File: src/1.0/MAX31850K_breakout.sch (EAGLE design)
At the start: 15 parts, among them J1 M08SQ1, U1 3.3V, U2 MAX31850K

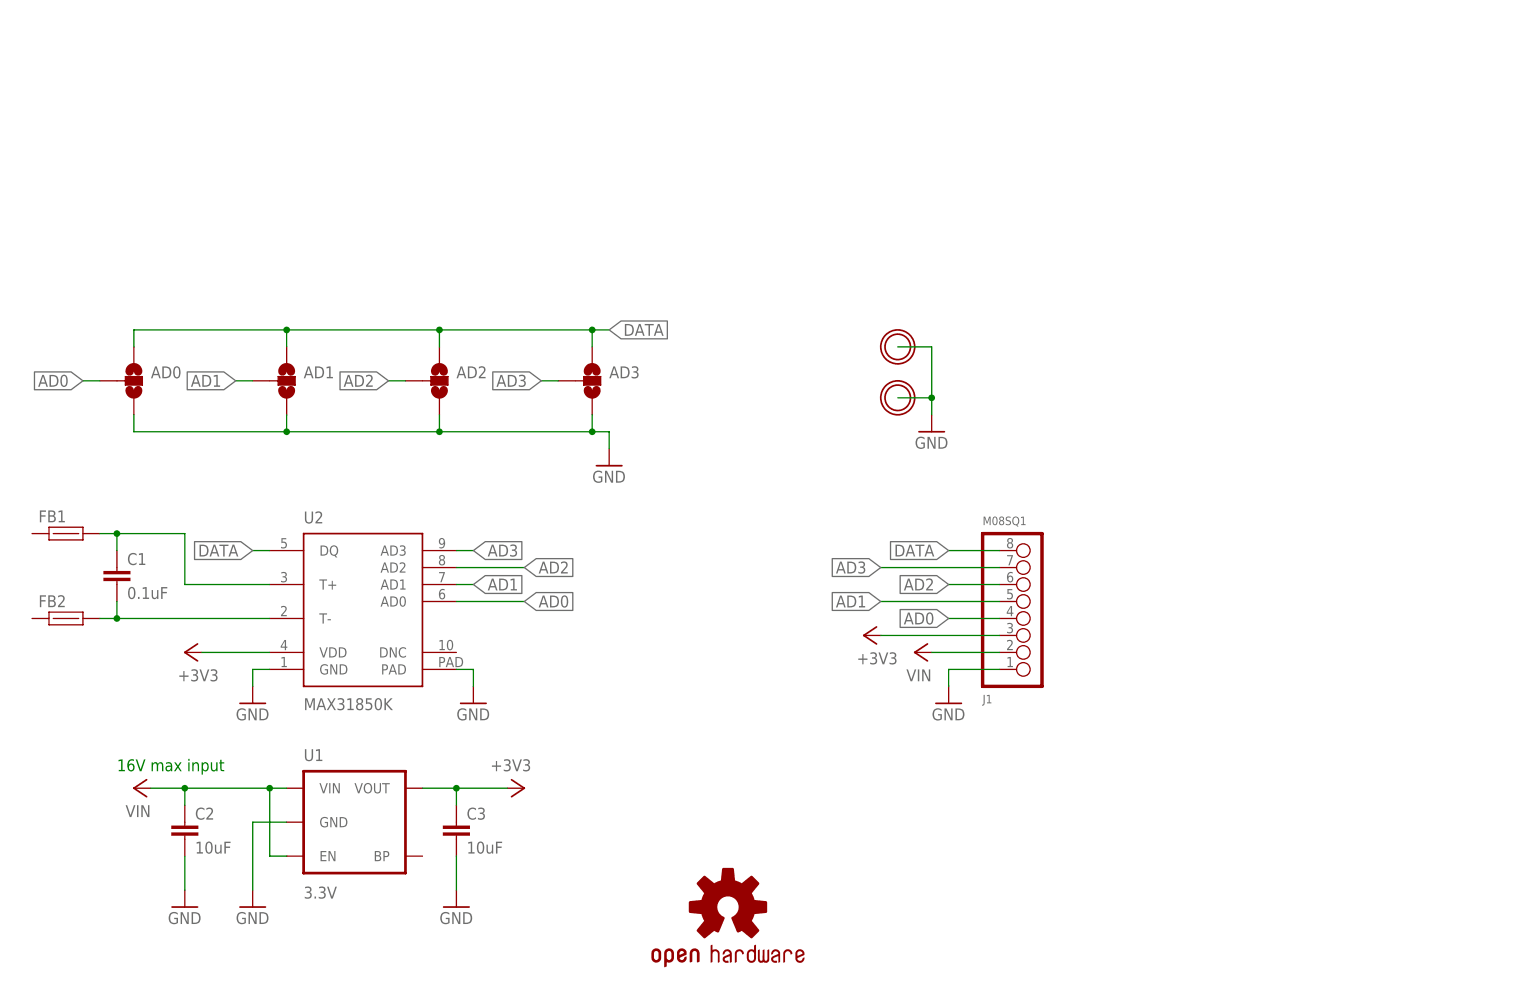
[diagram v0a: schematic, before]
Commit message: Updated file structure to match PCBGuidelines structure (still in development). Preparing to move to release candidate.
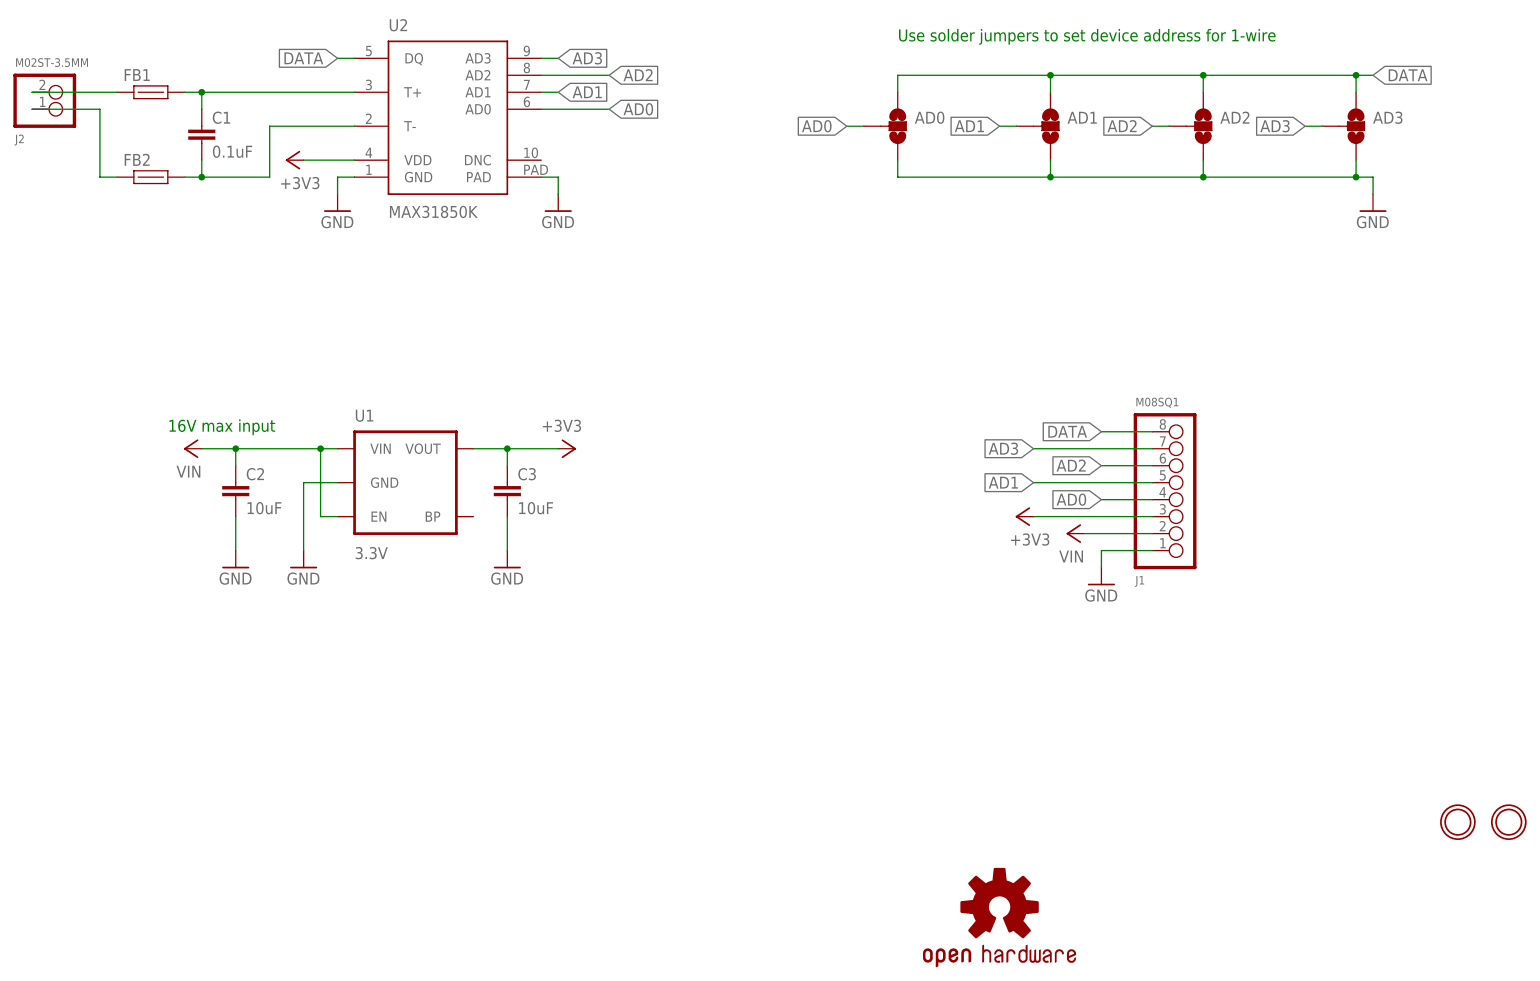
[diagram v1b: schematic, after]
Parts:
- added J2: M02ST-3.5MM, LoganSmith-Connectors:M02ST-3.5MM
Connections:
- new net TM_RAW: FB2.1, J2.1
- new net TP_RAW: FB1.1, J2.2
- net GND: no longer U$1.P$1, U$2.P$1
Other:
- note added: "Use solder jumpers to set device address for 1-wire"
- moved on the sheet: AD0, AD1, AD2, AD3, C1, C2, C3, FB1, FB2, J1, U1, U2

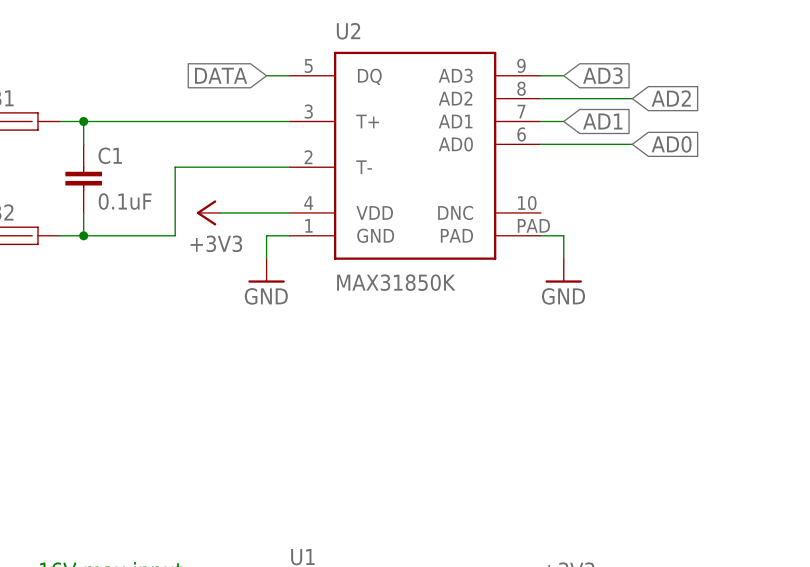
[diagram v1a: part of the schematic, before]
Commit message: Added BOM, still need part number for 1x8 header.
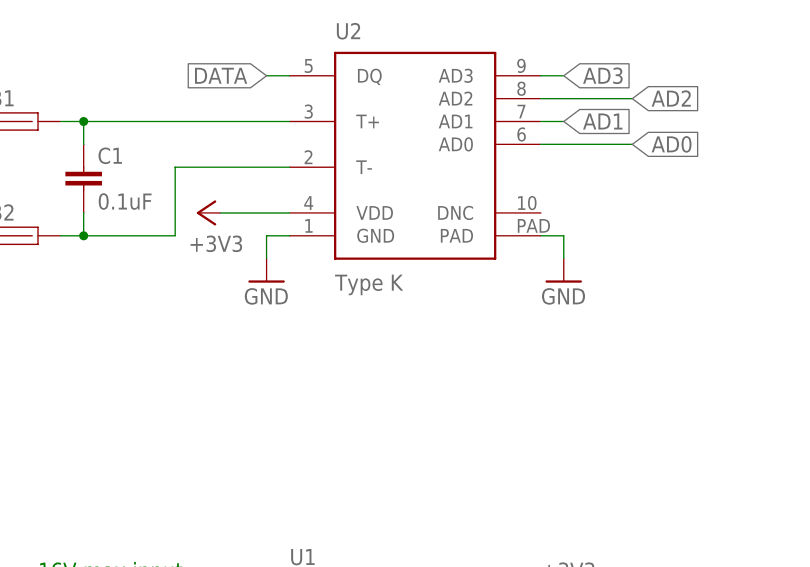
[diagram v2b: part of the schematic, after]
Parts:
- U2: value MAX31850K -> Type K; device LoganSmith-Digital_IC:MAX31850K -> LoganSmith-Analog_IC:MAX31850K
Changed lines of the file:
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@@
 <part name="GND5" library="supply1" deviceset="GND" device=""/>
 <part name="GND6" library="supply1" deviceset="GND" device=""/>
-<part name="U2" library="LoganSmith-Digital_IC" deviceset="MAX3185?*" device="0" technology="K"/>
+<part name="U2" library="LoganSmith-Analog_IC" deviceset="MAX3185?*" device="0" technology="K" value="Type K"/>
 <part name="J1" library="LoganSmith-Connectors" deviceset="M08?" device="SQ1"/>
 <part name="GND2" library="supply1" deviceset="GND" device=""/>
